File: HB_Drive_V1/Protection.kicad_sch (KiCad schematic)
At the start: 52 parts, among them SW1 SW_Push, SW2 SW_Push, U12 TL082, U13 TL082, U14 LM311, U15 TL082, U16 74AUC2G02, U17 74AUC2G02, U18 74LS08, U19 74LS32, U23 REF102CU, U5 74LS08

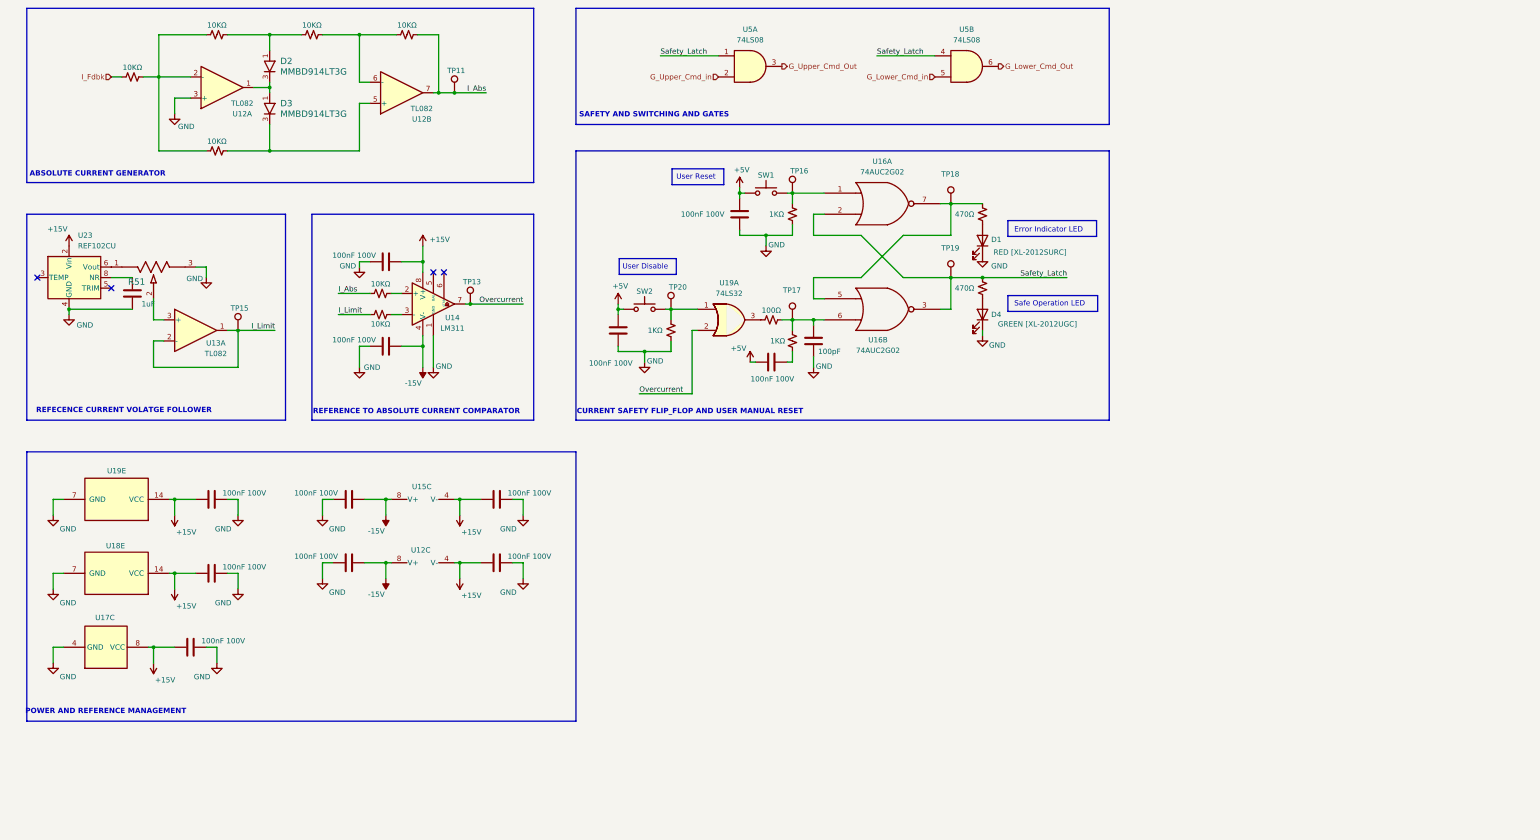
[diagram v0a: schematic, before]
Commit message: finishes hirearchical labels, add 10v +- ref generation and updates the DC offset circuits
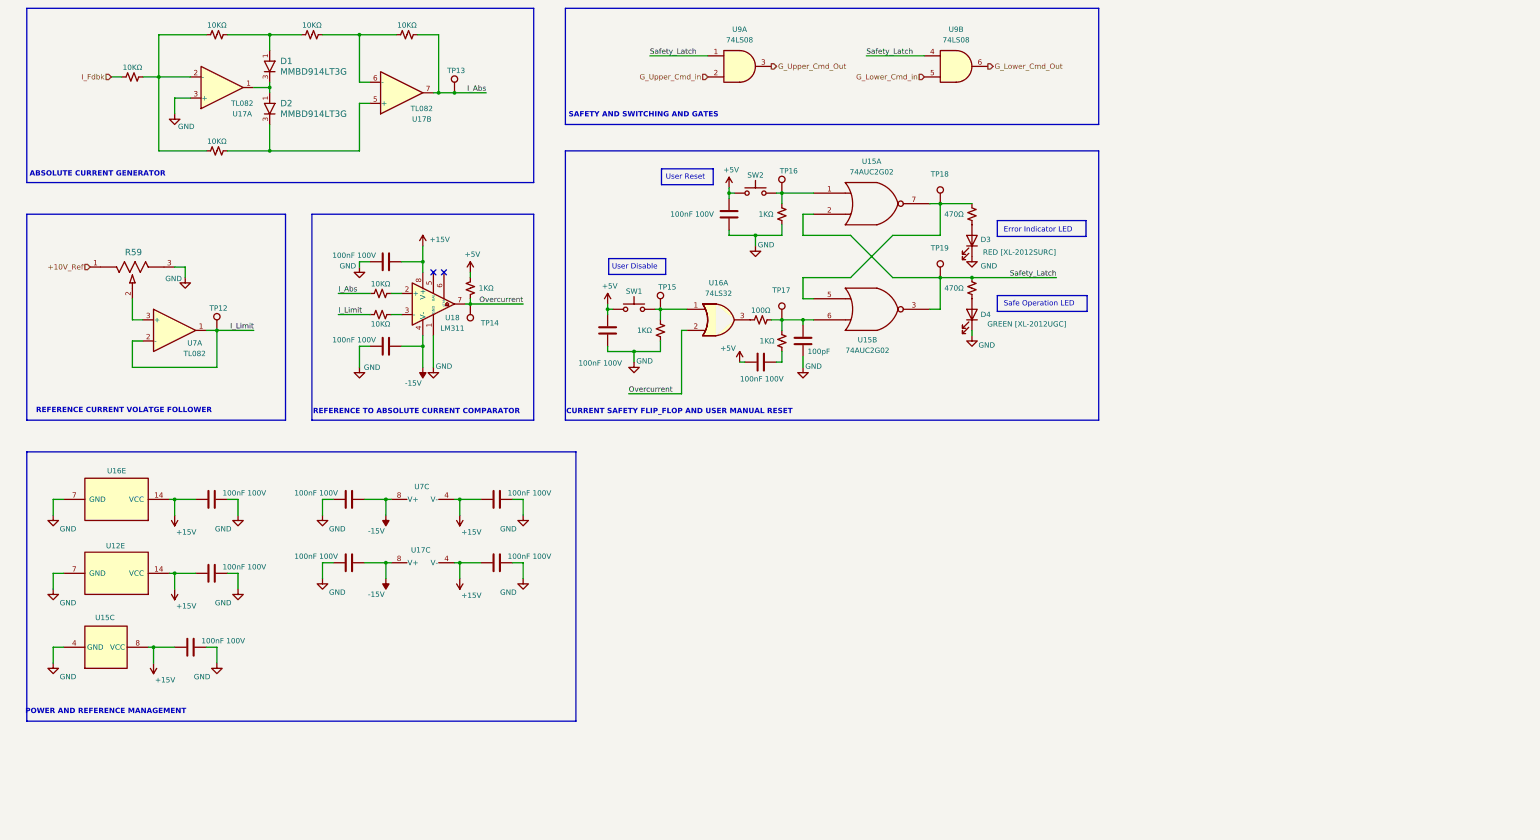
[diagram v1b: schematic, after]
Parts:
- removed C46: 1uF, Capacitor_SMD:C_0603_1608Metric, symbol Device:C
- removed U23: REF102CU, Package_SO:SOIC-8_3.9x4.9mm_P1.27mm, symbol Reference_Voltage:REF102CU
- added R88: 1KΩ, Resistor_SMD:R_0603_1608Metric_Pad0.98x0.95mm_HandSolder, symbol Device:R_Small_US
- renumbered C36 to C28, C38 to C29, C37 to C30, C25 to C31, C26 to C32, C28 to C33, C29 to C34, C34 to C35, C35 to C36, C33 to C37, C30 to C38, C31 to C39, C32 to C40, D2 to D1, D3 to D2, D1 to D3, R51 to R59, R25 to R60, R26 to R61, R27 to R62, R47 to R63, R60 to R64, R61 to R65, R48 to R66, R63 to R68, R62 to R69, R64 to R70, R66 to R71, R65 to R72, SW2 to SW1, SW1 to SW2, TP15 to TP12, TP11 to TP13, TP13 to TP14, TP20 to TP15, U18 to U12, U16 to U15, U17 to U15, U19 to U16, U12 to U17, U14 to U18, U13 to U7, U15 to U7, U5 to U9
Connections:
- net +5V: now also R88.2
- net Overcurrent: now also R88.1
- net +10V_Ref: now reaches R59.1
- no-connect marks 4 -> 2
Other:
- note added: "REFERENCE CURRENT VOLATGE FOLLOWER"
- note removed: "REFECENCE CURRENT VOLATGE FOLLOWER"
- moved on the sheet: D3, D4, R59, SW1, SW2, TP12, TP14, TP15, TP16, TP17, TP18, TP19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

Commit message: updates board to highest working copy
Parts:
- removed C30, C32, C36, C39: 100nF 100V, Capacitor_SMD:C_0603_1608Metric, symbol Device:C
- removed R70: 1KΩ, Resistor_SMD:R_0603_1608Metric_Pad0.98x0.95mm_HandSolder, symbol Device:R_Small_US
- removed TP17: TestPoint, TestPoint:TestPoint_Loop_D2.60mm_Drill1.6mm_Beaded, symbol Connector:TestPoint
- removed U12: 74LS08, symbol 74xx:74LS08
- removed unit 2 of U15
- removed unit 3 of U17
- removed U18: LM311, symbol Comparator:LM311
- added C703, C705: 100nF 100V, Capacitor_SMD:C_0603_1608Metric, symbol Device:C
- added J701, J702: Conn_02x02_Odd_Even, Connector_PinHeader_2.54mm:PinHeader_2x02_P2.54mm_Vertical, symbol Connector_Generic:Conn_02x02_Odd_Even
- added R713: 1KΩ, Resistor_SMD:R_0603_1608Metric_Pad0.98x0.95mm_HandSolder, symbol Device:R_Small_US
- added TP706: TestPoint, TestPoint:TestPoint_Loop_D2.60mm_Drill1.6mm_Beaded, symbol Connector:TestPoint
- added unit 2 of U701
- added unit 3 of U704
- added U705: LM311, Package_SO:SOIC-8_3.9x4.9mm_P1.27mm, symbol Comparator:LM311
- U402: renamed from U9; footprint (none) -> Package_SO:SOIC-14_3.9x8.7mm_P1.27mm
- U701: renamed from U15; footprint (none) -> Package_SO:VSSOP-8_2.3x2mm_P0.5mm
- renumbered C28 to C701, C29 to C702, C31 to C704, C33 to C706, C34 to C707, C35 to C708, C37 to C710, C38 to C711, C40 to C712, D1 to D701, D2 to D702, D3 to D703, D4 to D704, R59 to R701, R60 to R702, R61 to R703, R62 to R704, R63 to R705, R64 to R706, R65 to R707, R66 to R708, R88 to R709, R67 to R710, R68 to R711, R69 to R712, R71 to R714, R72 to R715, SW1 to SW701, SW2 to SW702, TP12 to TP701, TP13 to TP702, TP14 to TP703, TP15 to TP704, TP16 to TP705, TP18 to TP707, TP19 to TP708, U16 to U702, U17 to U703, U7 to U703, U7 to U704
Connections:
- net +15V: now also C704.1, U703.8 (V+), C703.1, U704.8 (V+), U705.8 (V+); no longer C701.2, C702.2, C708.2, U701.8 (VCC), U702.14 (VCC), U703.4 (V-)
- net +5V: now also C701.2, C702.2, U701.8 (VCC), U702.14 (VCC), J701.1 (Pin_1), J702.1 (Pin_1), R713.2
- net -15V: now also C708.2, U703.4 (V-), C705.2, U704.4 (V-), U705.4 (V-); no longer C704.1, U703.8 (V+)
- net GND: now also C703.2, C705.1, U705.1 (GND)
- net G_Lower_Cmd_Out: now also U402.11; no longer U402.6
- net G_Lower_Cmd_in: now also U402.13; no longer U402.5
- net G_Upper_Cmd_Out: now also U402.8; no longer U402.3
- net G_Upper_Cmd_in: now also U402.10; no longer U402.2
- net Overcurrent: now also U705.7
- net Safety_Latch: now also J701.3 (Pin_3), J702.3 (Pin_3), U701.3; no longer U402.1, U402.4
- net at R714.2, TP707.1, U701.7: now also U701.5
- net at C712.2, R711.2: now also R713.1, TP706.1, U701.6
- net at R706.2: now also U705.2 (+)
- net at R707.1: now also U705.3 (-)
- net I_Fdbk renamed I_Fdbk_Raw
- new net: J701.2 (Pin_2), J701.4 (Pin_4), U402.9
- new net: J702.2 (Pin_2), J702.4 (Pin_4), U402.12
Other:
- moved on the sheet: D701, D702, D703, D704, R701, SW701, SW702, TP701, TP702, TP703, TP704, TP705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

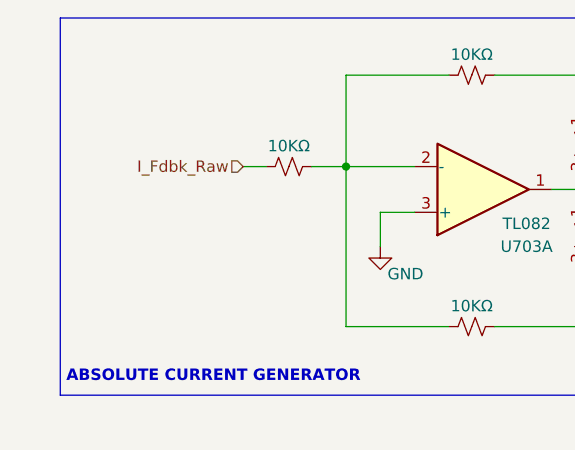
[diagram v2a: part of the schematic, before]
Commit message: removes Aux file trouble
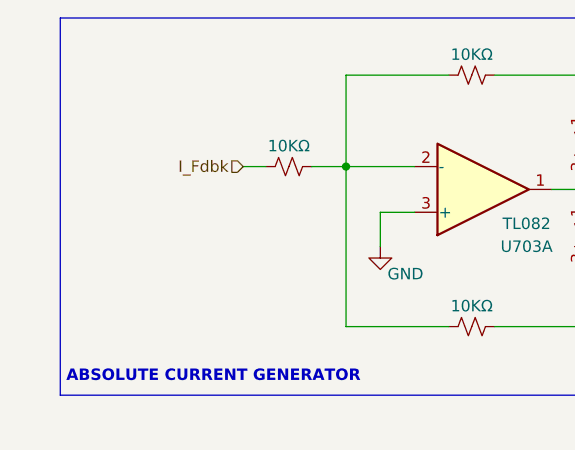
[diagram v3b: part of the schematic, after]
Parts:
- U703, U704: footprint Package_SO:SOIC-8_5.3x5.3mm_P1.27mm -> Package_SO:SOIC-8_3.9x4.9mm_P1.27mm
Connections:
- net I_Fdbk_Raw renamed I_Fdbk
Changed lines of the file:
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@@
 		)
 	)
-	(hierarchical_label "I_Fdbk_Raw"
+	(hierarchical_label "I_Fdbk"
 		(shape input)
 		(at 115.57 76.2 180)
@@
 			)
 		)
-		(property "Footprint" "Package_SO:SOIC-8_5.3x5.3mm_P1.27mm"
+		(property "Footprint" "Package_SO:SOIC-8_3.9x4.9mm_P1.27mm"
 			(at 142.24 78.74 0)
 			(hide yes)
@@
 			)
 		)
-		(property "Footprint" "Package_SO:SOIC-8_5.3x5.3mm_P1.27mm"
+		(property "Footprint" "Package_SO:SOIC-8_3.9x4.9mm_P1.27mm"
 			(at 185.42 80.01 0)
 			(hide yes)
@@
 			)
 		)
-		(property "Footprint" "Package_SO:SOIC-8_5.3x5.3mm_P1.27mm"
+		(property "Footprint" "Package_SO:SOIC-8_3.9x4.9mm_P1.27mm"
 			(at 130.81 137.16 0)
 			(hide yes)
@@
 			)
 		)
-		(property "Footprint" "Package_SO:SOIC-8_5.3x5.3mm_P1.27mm"
+		(property "Footprint" "Package_SO:SOIC-8_3.9x4.9mm_P1.27mm"
 			(at 191.77 199.39 0)
 			(hide yes)
@@
 			)
 		)
-		(property "Footprint" "Package_SO:SOIC-8_5.3x5.3mm_P1.27mm"
+		(property "Footprint" "Package_SO:SOIC-8_3.9x4.9mm_P1.27mm"
 			(at 190.5 179.07 0)
 			(hide yes)

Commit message: commits latest kiCAD project for BOM generation
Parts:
- removed SW701, SW702: SW_Push, symbol Switch:SW_Push
- added SW701, SW704: PTS636SL43SMTRLFS, PTS636SL43SMTRLFS:PTS636SL43SMTRLFS, symbol PTS636SL43SMTRLFS:PTS636SL43SMTRLFS
- D701, D702: footprint Package_TO_SOT_SMD:SOT-23-3 -> SOT-23_ONS
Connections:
- net +5V: now also SW701.1, SW704.1
- net at R712.2, TP705.1, U701.1: now also SW704.2
- net at R710.2, TP704.1, U702.1: now also SW701.2
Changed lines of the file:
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@@
 	(wire
 		(pts
-			(xy 234.95 132.08) (xy 236.22 132.08)
-		)
-		(stroke
-			(width 0)
-			(type default)
-		)
-	)
-	(wire
-		(pts
 			(xy 127 76.2) (xy 134.62 76.2)
 		)
@@
 	(wire
 		(pts
-			(xy 246.38 132.08) (xy 247.65 132.08)
-		)
-		(stroke
-			(width 0)
-			(type default)
-		)
-	)
-	(wire
-		(pts
 			(xy 247.65 134.62) (xy 247.65 132.08)
 		)
@@
 	(wire
 		(pts
-			(xy 264.16 104.14) (xy 265.43 104.14)
-		)
-		(stroke
-			(width 0)
-			(type default)
-		)
-	)
-	(wire
-		(pts
 			(xy 309.88 68.58) (xy 309.88 71.12)
 		)
@@
 	(wire
 		(pts
-			(xy 275.59 104.14) (xy 276.86 104.14)
-		)
-		(stroke
-			(width 0)
-			(type default)
-		)
-	)
-	(wire
-		(pts
 			(xy 166.37 181.61) (xy 168.91 181.61)
 		)
@@
 	)
 	(symbol
-		(lib_name "MMBD914LT3G_1")
 		(lib_id "MMBD914LT3G:MMBD914LT3G")
 		(at 153.67 73.66 270)
@@
 			)
 		)
-		(property "Footprint" "Package_TO_SOT_SMD:SOT-23-3"
+		(property "Footprint" "SOT-23_ONS"
 			(at 153.67 64.77 0)
 			(hide yes)
@@
 	)
 	(symbol
-		(lib_id "Switch:SW_Push")
-		(at 241.3 132.08 0)
-		(unit 1)
-		(body_style 1)
-		(exclude_from_sim no)
-		(in_bom yes)
-		(on_board yes)
-		(in_pos_files yes)
-		(dnp no)
-		(property "Reference" "SW701"
-			(at 241.3 127.762 0)
-			(show_name no)
-			(do_not_autoplace no)
-			(effects
-				(font
-					(size 1.27 1.27)
-				)
-			)
-		)
-		(property "Value" "SW_Push"
-			(at 239.522 120.65 0)
-			(hide yes)
-			(show_name no)
-			(do_not_autoplace no)
-			(effects
-				(font
-					(size 1.27 1.27)
-				)
-			)
-		)
-		(property "Footprint" ""
-			(at 241.3 127 0)
-			(hide yes)
-			(show_name no)
-			(do_not_autoplace no)
-			(effects
-				(font
-					(size 1.27 1.27)
-				)
-			)
-		)
-		(property "Datasheet" ""
-			(at 241.3 127 0)
-			(hide yes)
-			(show_name no)
-			(do_not_autoplace no)
-			(effects
-				(font
-					(size 1.27 1.27)
-				)
-			)
-		)
-		(property "Description" "Push button switch, generic, two pins"
-			(at 241.3 132.08 0)
-			(hide yes)
-			(show_name no)
-			(do_not_autoplace no)
-			(effects
-				(font
-					(size 1.27 1.27)
-				)
-			)
-		)
-		(pin "2"
-		)
-		(pin "1"
-		)
-		(instances
-			(project "HB_Drive_V1"
-				(path "/a9b54c89-4c8e-4c90-8a0d-ec2009e369b7/28e2d9d3-ebce-4623-8c7e-52f93025d826/cc6479ca-50da-4dbe-9d7f-2e2b1563a3b2"
-					(reference "SW701")
-					(unit 1)
-				)
-			)
-		)
-	)
-	(symbol
 		(lib_id "power:GND")
 		(at 130.81 85.09 0)
@@
 	)
 	(symbol
-		(lib_name "MMBD914LT3G_1")
 		(lib_id "MMBD914LT3G:MMBD914LT3G")
 		(at 153.67 83.82 270)
@@
 			)
 		)
-		(property "Footprint" "Package_TO_SOT_SMD:SOT-23-3"
+		(property "Footprint" "SOT-23_ONS"
 			(at 153.67 74.93 0)
 			(hide yes)
@@
 	)
 	(symbol
+		(lib_id "PTS636SL43SMTRLFS:PTS636SL43SMTRLFS")
+		(at 262.89 104.14 0)
+		(unit 1)
+		(body_style 1)
+		(exclude_from_sim no)
+		(in_bom yes)
+		(on_board yes)
+		(in_pos_files yes)
+		(dnp no)
+		(property "Reference" "SW704"
+			(at 270.764 100.584 0)
+			(show_name no)
+			(do_not_autoplace no)
+			(effects
+				(font
+					(size 1.524 1.524)
+				)
+			)
+		)
+		(property "Value" "PTS636SL43SMTRLFS"
+			(at 270.51 100.33 0)
+			(hide yes)
+			(show_name no)
+			(do_not_autoplace no)
+			(effects
+				(font
+					(size 1.524 1.524)
+				)
+			)
+		)
+		(property "Footprint" "PTS636SL43SMTRLFS:PTS636SL43SMTRLFS"
+			(at 262.89 104.14 0)
+			(hide yes)
+			(show_name no)
+			(do_not_autoplace no)
+			(effects
+				(font
+					(size 1.27 1.27)
+					(italic yes)
+				)
+			)
+		)
+		(property "Datasheet" "PTS636SL43SMTRLFS"
+			(at 262.89 104.14 0)
+			(hide yes)
+			(show_name no)
+			(do_not_autoplace no)
+			(effects
+				(font
+					(size 1.27 1.27)
+					(italic yes)
+				)
+			)
+		)
+		(property "Description" ""
+			(at 262.89 104.14 0)
+			(hide yes)
+			(show_name no)
+			(do_not_autoplace no)
+			(effects
+				(font
+					(size 1.27 1.27)
+				)
+			)
+		)
+		(pin "2"
+		)
+		(pin "1"
+		)
+		(instances
+			(project "HB_Drive_V1"
+				(path "/a9b54c89-4c8e-4c90-8a0d-ec2009e369b7/28e2d9d3-ebce-4623-8c7e-52f93025d826/cc6479ca-50da-4dbe-9d7f-2e2b1563a3b2"
+					(reference "SW704")
+					(unit 1)
+				)
+			)
+		)
+	)
+	(symbol
 		(lib_id "power:-15V")
 		(at 200.66 199.39 0)
@@
 	)
 	(symbol
-		(lib_id "Switch:SW_Push")
-		(at 270.51 104.14 0)
-		(unit 1)
-		(body_style 1)
-		(exclude_from_sim no)
-		(in_bom yes)
-		(on_board yes)
-		(in_pos_files yes)
-		(dnp no)
-		(property "Reference" "SW702"
-			(at 270.51 99.822 0)
-			(show_name no)
-			(do_not_autoplace no)
-			(effects
-				(font
-					(size 1.27 1.27)
-				)
-			)
-		)
-		(property "Value" "SW_Push"
-			(at 268.732 92.71 0)
-			(hide yes)
-			(show_name no)
-			(do_not_autoplace no)
-			(effects
-				(font
-					(size 1.27 1.27)
-				)
-			)
-		)
-		(property "Footprint" ""
-			(at 270.51 99.06 0)
-			(hide yes)
-			(show_name no)
-			(do_not_autoplace no)
-			(effects
-				(font
-					(size 1.27 1.27)
-				)
-			)
-		)
-		(property "Datasheet" ""
-			(at 270.51 99.06 0)
-			(hide yes)
-			(show_name no)
-			(do_not_autoplace no)
-			(effects
-				(font
-					(size 1.27 1.27)
-				)
-			)
-		)
-		(property "Description" "Push button switch, generic, two pins"
-			(at 270.51 104.14 0)
-			(hide yes)
-			(show_name no)
-			(do_not_autoplace no)
-			(effects
-				(font
-					(size 1.27 1.27)
-				)
-			)
-		)
-		(pin "2"
-		)
-		(pin "1"
-		)
-		(instances
-			(project "HB_Drive_V1"
-				(path "/a9b54c89-4c8e-4c90-8a0d-ec2009e369b7/28e2d9d3-ebce-4623-8c7e-52f93025d826/cc6479ca-50da-4dbe-9d7f-2e2b1563a3b2"
-					(reference "SW702")
-					(unit 1)
-				)
-			)
-		)
-	)
-	(symbol
 		(lib_id "power:GND")
 		(at 281.94 146.05 0)
@@
 					(unit 1)
 				)
+			)
+		)
+	)
+	(symbol
+		(lib_id "PTS636SL43SMTRLFS:PTS636SL43SMTRLFS")
+		(at 233.68 132.08 0)
+		(unit 1)
+		(body_style 1)
+		(exclude_from_sim no)
+		(in_bom yes)
+		(on_board yes)
+		(in_pos_files yes)
+		(dnp no)
+		(property "Reference" "SW701"
+			(at 241.554 128.524 0)
+			(show_name no)
+			(do_not_autoplace no)
+			(effects
+				(font
+					(size 1.524 1.524)
+				)
+			)
+		)
+		(property "Value" "PTS636SL43SMTRLFS"
+			(at 241.3 128.27 0)
+			(hide yes)
+			(show_name no)
+			(do_not_autoplace no)
+			(effects
+				(font
+					(size 1.524 1.524)
+				)
+			)
+		)
+		(property "Footprint" "PTS636SL43SMTRLFS:PTS636SL43SMTRLFS"
+			(at 233.68 132.08 0)
+			(hide yes)
+			(show_name no)
+			(do_not_autoplace no)
+			(effects
+				(font
+					(size 1.27 1.27)
+					(italic yes)
+				)
+			)
+		)
+		(property "Datasheet" "PTS636SL43SMTRLFS"
+			(at 233.68 132.08 0)
+			(hide yes)
+			(show_name no)
+			(do_not_autoplace no)
+			(effects
+				(font
+					(size 1.27 1.27)
+					(italic yes)
+				)
+			)
+		)
+		(property "Description" ""
+			(at 233.68 132.08 0)
+			(hide yes)
+			(show_name no)
+			(do_not_autoplace no)
+			(effects
+				(font
+					(size 1.27 1.27)
+				)
+			)
+		)
+		(pin "2"
+		)
+		(pin "1"
+		)
+		(instances
+			(project "HB_Drive_V1"
+				(path "/a9b54c89-4c8e-4c90-8a0d-ec2009e369b7/28e2d9d3-ebce-4623-8c7e-52f93025d826/cc6479ca-50da-4dbe-9d7f-2e2b1563a3b2"
+					(reference "SW701")
+					(unit 1)
+				)

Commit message: updates board to REV 1 Ordered version
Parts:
- added unit 2 of U702
- added unit 3 of U702
- added unit 4 of U702
- added unit 2 of U704
- D703: value RED [XL-2012SURC] -> LTST-C170KRKT [RED]
- D704: value GREEN [XL-2012UGC] -> LTST-C170KGKT [GREEN]
- R702, R703, R704, R705, R706, R707, R708: value 10KΩ -> 10kΩ 1%
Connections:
- net +5V: now also U702.10, U702.12, U702.13, U702.4, U702.5, U702.9
- net GND: now also U704.5 (+)
- new net: U704.6 (-), U704.7
- no-connect marks 2 -> 5
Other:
- note added: "unused ANDS 702B-D on 74LS32 Quad Package"
- note added: "unused OpAmp 704B on TL082 Dual Package"
- moved on the sheet: R701, TP701, U704A
